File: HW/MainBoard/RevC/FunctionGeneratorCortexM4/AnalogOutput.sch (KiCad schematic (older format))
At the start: 31 parts, among them U12 TL072, U13 TL072, U5 THS7002, U9 TS12A12511DCNR

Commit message: Updated MainBoard RevC
- Block diagram and connections completed on schematic
- Need to check MCU pin availability
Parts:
- removed JP? (x2): Jumper_NO_Small, symbol Device:Jumper_NO_Small
- removed U5: THS7002, symbol PGA:THS7002
- added C13, C9: 100nF, Capacitor_SMD:C_1206_3216Metric_Pad1.42x1.75mm_HandSolder, symbol Device:C
- added C14: 10uF, Capacitor_SMD:CP_Elec_4x5.7, symbol Device:CP
- added D3, D7: D_TVS, symbol Device:D_TVS
- added R12, R13: 10K, Resistor_SMD:R_1206_3216Metric_Pad1.42x1.75mm_HandSolder, symbol Device:R
- added R16, R19, R22, R32: 1K, Resistor_SMD:R_0805_2012Metric_Pad1.15x1.40mm_HandSolder, symbol Device:R
- added R25, R33: 2K2, Resistor_SMD:R_0805_2012Metric_Pad1.15x1.40mm_HandSolder, symbol Device:R
- added R26, R34: 2K7, Resistor_SMD:R_0805_2012Metric_Pad1.15x1.40mm_HandSolder, symbol Device:R
- added R27, R35: 3K3, Resistor_SMD:R_0805_2012Metric_Pad1.15x1.40mm_HandSolder, symbol Device:R
- added R28, R36: 3K9, Resistor_SMD:R_0805_2012Metric_Pad1.15x1.40mm_HandSolder, symbol Device:R
- added R29, R37: 4K7, Resistor_SMD:R_0805_2012Metric_Pad1.15x1.40mm_HandSolder, symbol Device:R
- added R30, R38: 5K6, Resistor_SMD:R_0805_2012Metric_Pad1.15x1.40mm_HandSolder, symbol Device:R
- added R31, R39: 6K8, Resistor_SMD:R_0805_2012Metric_Pad1.15x1.40mm_HandSolder, symbol Device:R
- added R6: 560R, Resistor_SMD:R_1206_3216Metric_Pad1.42x1.75mm_HandSolder, symbol Device:R
- added TP1: TestPoint, TestPoint:TestPoint_Pad_1.0x1.0mm, symbol Connector:TestPoint
- added U10: TS5A21366, Package_SO:VSSOP-8_2.4x2.1mm_P0.5mm, symbol Analog_Switch:MAX323CPA
- added U11, U16: CD4051B, symbol Analog_Switch:CD4051B
- added U14, U15, U2, U5: DG470_1, Package_SO:MSOP-8_3x3mm_P0.65mm, symbol DG470:DG470_1
- added U7: TL072, symbol Amplifier_Operational:TL072
- gave numbers to parts that had none: 3
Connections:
- net labels added: CH1_GAIN_A, CH1_GAIN_B, CH1_GAIN_C, CH1_INVERT_MUX, CH1_OFFSET_MUX, CH1_SIGNAL, CH1_SIGNAL_OUT, CH2_GAIN_A, CH2_GAIN_B, CH2_GAIN_C, CH2_INVERT_MUX, CH2_OFFSET_MUX, CH2_SIGNAL, CH2_SIGNAL_OUT
- net labels removed: FUNC1_SIG_IN, FUNC1_SIG_OUT, FUNC1_SYNC_IN, FUNC1_SYNC_OUT, GNDS, SG0_IN, SG1_IN, SG2_IN
- wire segments 129 -> 255
- no-connect marks 7 -> 1
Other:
- note added: "0V-3V3"
- note added: "ANALOG INVERTER\n"
- note added: "DC OFFSET"
- note added: "PROGRAMMABLE\nGAIN AMPLIFIER"
- moved on the sheet: C16, C21, C26, C33, C34, R1, R10, R14, R15, R17, R18, R2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

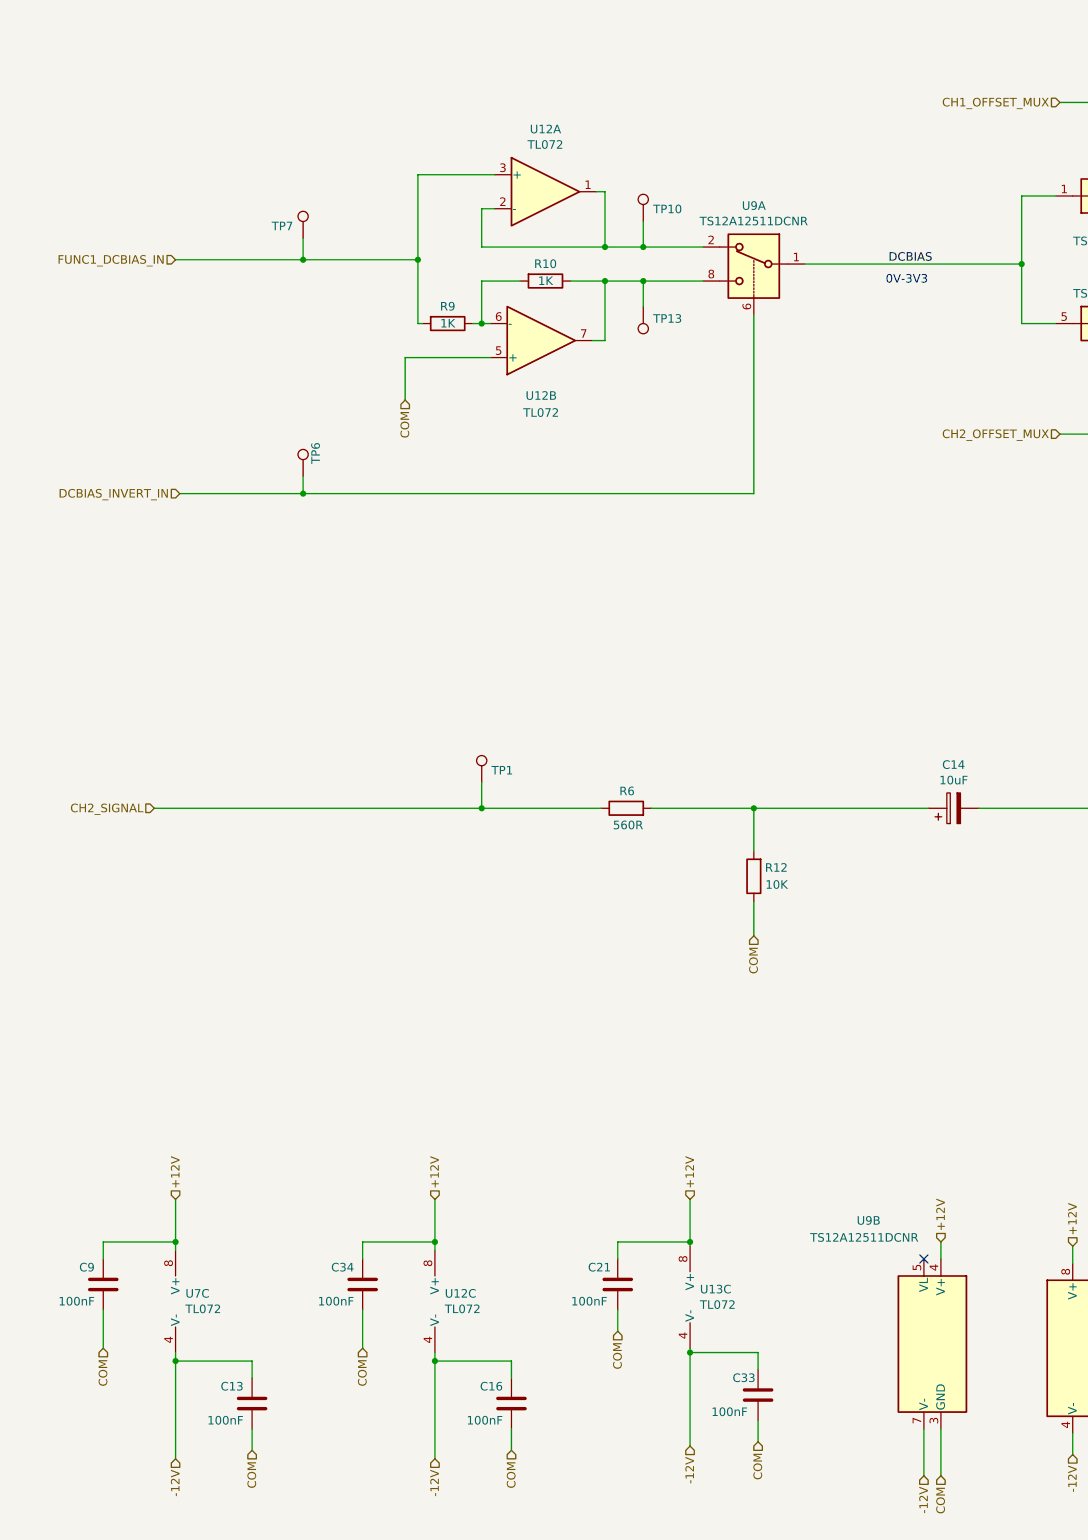
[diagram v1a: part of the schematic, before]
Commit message: Changed OFFSET SPDT to DG470
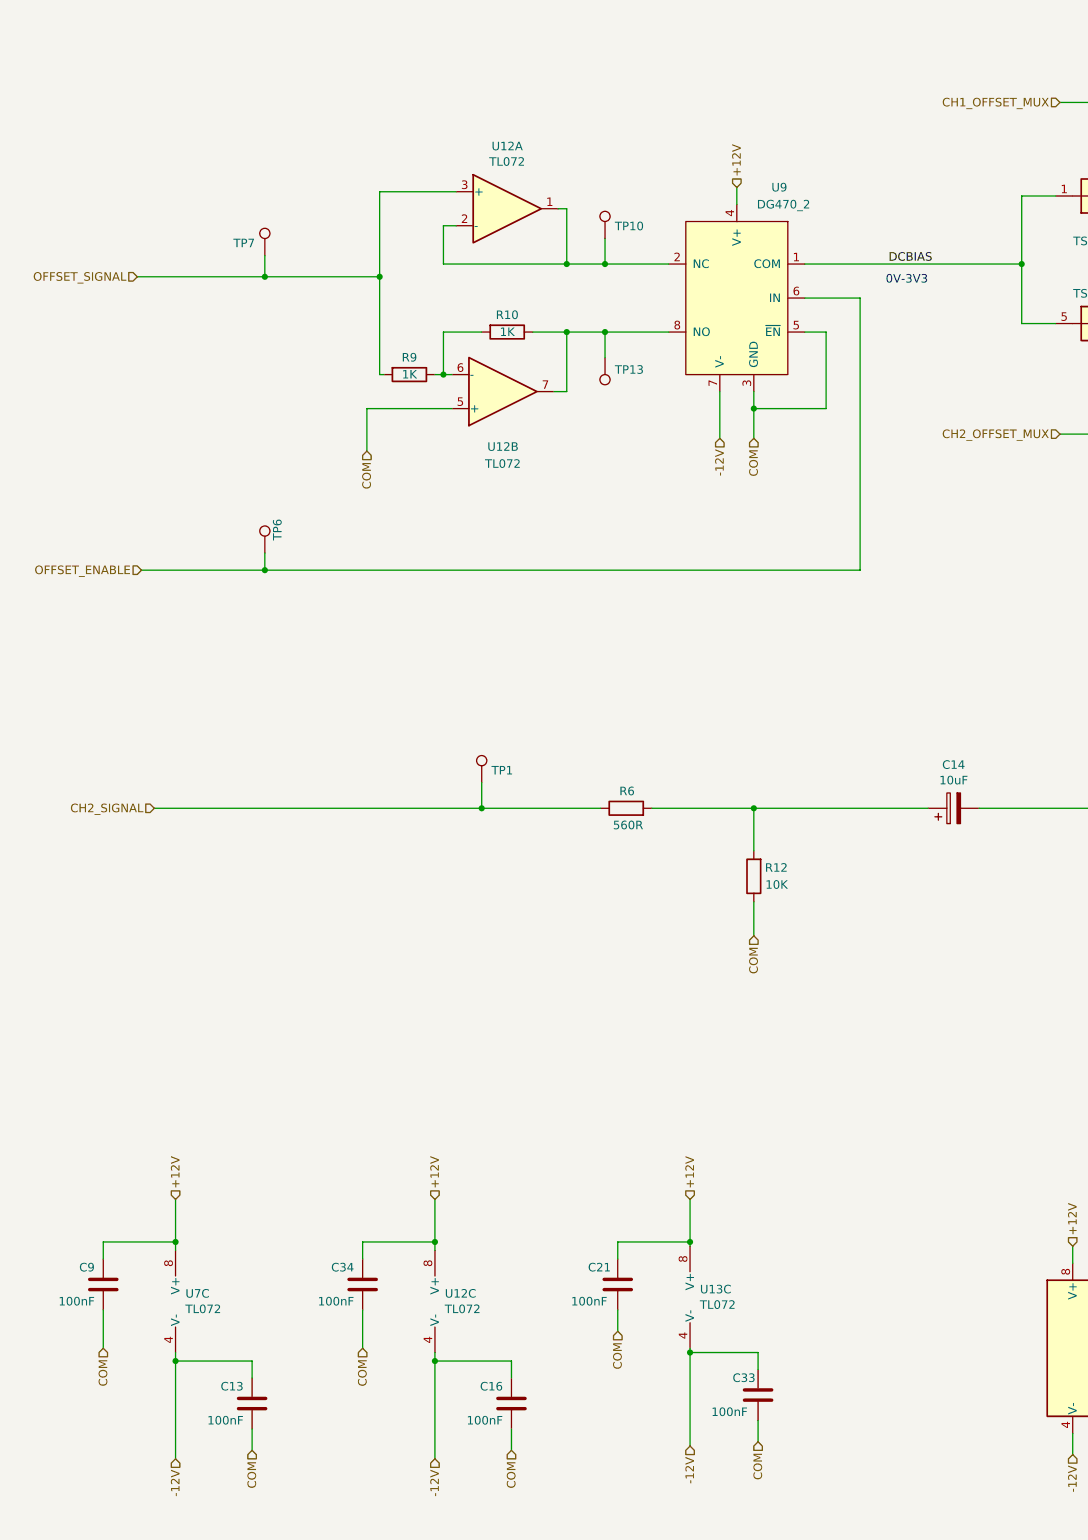
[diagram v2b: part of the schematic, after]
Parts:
- removed U9: TS12A12511DCNR, Package_TO_SOT_SMD:SOT-23-8_Handsoldering, symbol Analog_Switch:DG419LDJ
- added U9: DG470_2, Package_SO:MSOP-8_3x3mm_P0.65mm, symbol DG470:DG470_2
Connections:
- net +12V: now also U9.4 (V+)
- net -12V: now also U9.7 (V-)
- net COM: now also U9.3 (GND), U9.5 (~EN)
- net DCBIAS: now also U9.1 (COM)
- net at R10.1, TP13.1, U12.7: now also U9.8 (NO)
- net at TP10.1, U12.1, U12.2 (-): now also U9.2 (NC)
- net DCBIAS_INVERT_IN renamed OFFSET_ENABLE
- net OFFSET_ENABLE: now also U9.6 (IN)
- net FUNC1_DCBIAS_IN renamed OFFSET_SIGNAL
- no-connect marks 1 -> 0
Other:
- moved on the sheet: R10, R9, TP10, TP13, TP6, TP7, U12A, U12B

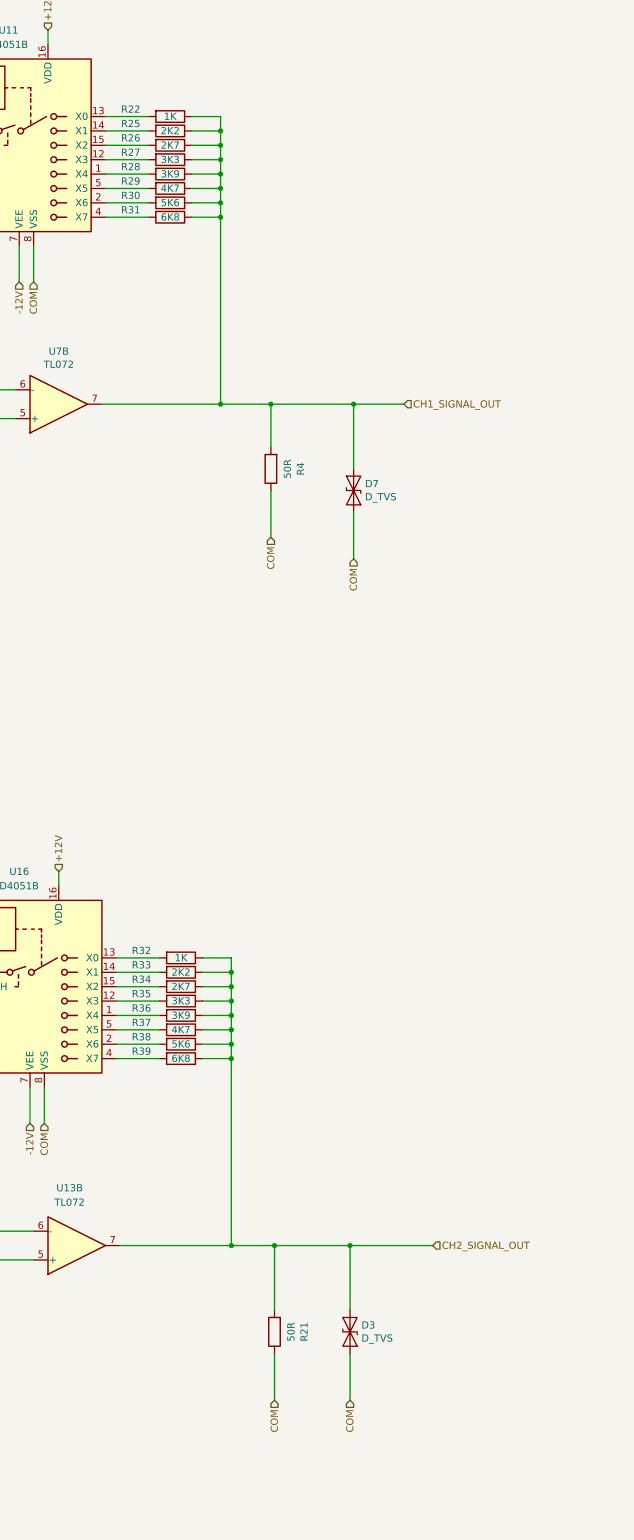
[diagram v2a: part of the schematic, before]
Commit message: Added two-series resistors in PGA feedback
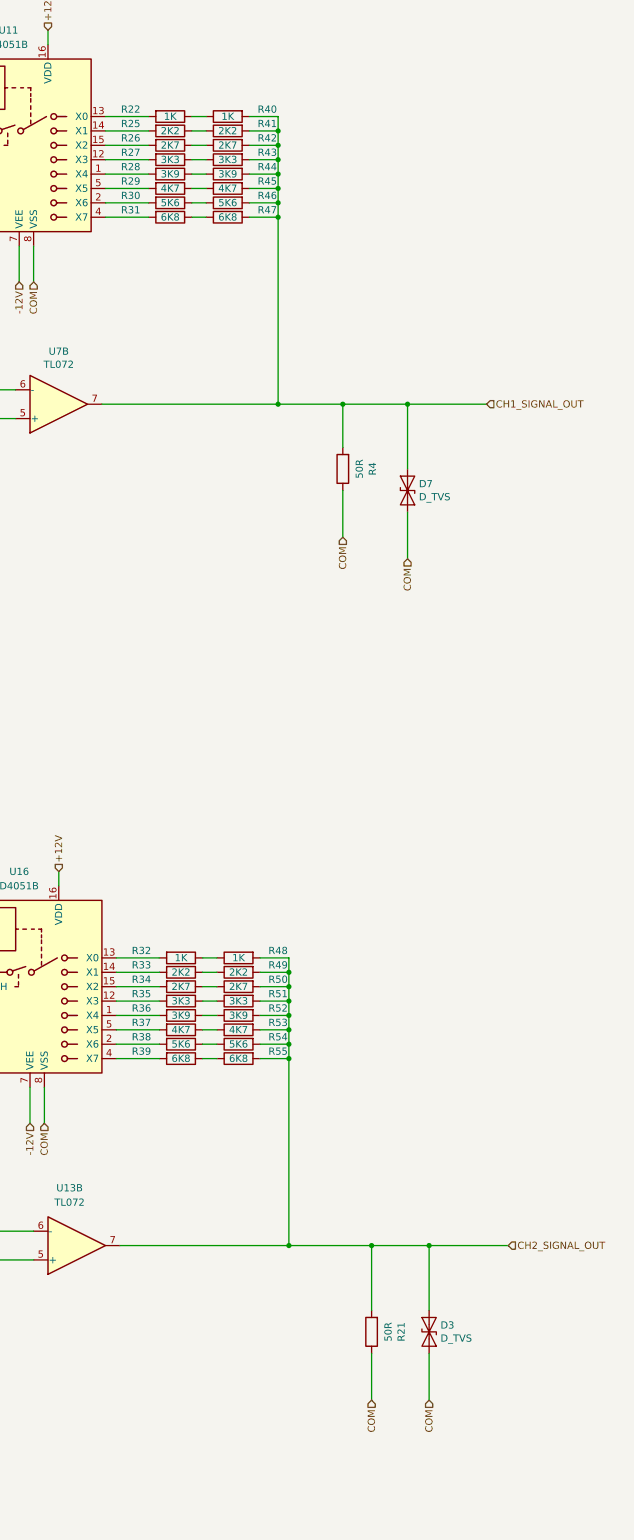
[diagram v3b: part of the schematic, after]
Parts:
- added R40, R48: 1K, Resistor_SMD:R_0805_2012Metric_Pad1.15x1.40mm_HandSolder, symbol Device:R
- added R41, R49: 2K2, Resistor_SMD:R_0805_2012Metric_Pad1.15x1.40mm_HandSolder, symbol Device:R
- added R42, R50: 2K7, Resistor_SMD:R_0805_2012Metric_Pad1.15x1.40mm_HandSolder, symbol Device:R
- added R43, R51: 3K3, Resistor_SMD:R_0805_2012Metric_Pad1.15x1.40mm_HandSolder, symbol Device:R
- added R44, R52: 3K9, Resistor_SMD:R_0805_2012Metric_Pad1.15x1.40mm_HandSolder, symbol Device:R
- added R45, R53: 4K7, Resistor_SMD:R_0805_2012Metric_Pad1.15x1.40mm_HandSolder, symbol Device:R
- added R46, R54: 5K6, Resistor_SMD:R_0805_2012Metric_Pad1.15x1.40mm_HandSolder, symbol Device:R
- added R47, R55: 6K8, Resistor_SMD:R_0805_2012Metric_Pad1.15x1.40mm_HandSolder, symbol Device:R
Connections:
- net CH1_SIGNAL_OUT: now also R40.2, R41.2, R42.2, R43.2, R44.2, R45.2, R46.2, R47.2; no longer R22.1, R25.1, R26.1, R27.1, R28.1, R29.1, R30.1, R31.1
- net CH2_SIGNAL_OUT: now also R48.2, R49.2, R50.2, R51.2, R52.2, R53.2, R54.2, R55.2; no longer R32.1, R33.1, R34.1, R35.1, R36.1, R37.1, R38.1, R39.1
- new net: R22.1, R40.1
- new net: R25.1, R41.1
- new net: R26.1, R42.1
- new net: R27.1, R43.1
- new net: R28.1, R44.1
- new net: R29.1, R45.1
- new net: R30.1, R46.1
- new net: R31.1, R47.1
- new net: R32.1, R48.1
- new net: R33.1, R49.1
- new net: R34.1, R50.1
- new net: R35.1, R51.1
- new net: R36.1, R52.1
- new net: R37.1, R53.1
- new net: R38.1, R54.1
- new net: R39.1, R55.1
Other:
- moved on the sheet: D3, D7, R21, R4

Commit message: Created RevE ControlBoard to use 2.54 SMD header
Header is at the top of the board to let buttons and encoder be closer together
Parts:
- removed unit 1 of U10
- removed unit 2 of U10
- added U? (x2): DG468DV_T1_E3, Package_SO:TSOP-6_1.65x3.05mm_P0.95mm, symbol DG46x:DG468DV_T1_E3
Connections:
- net +12V: now also U?.5 (V+), U?.5 (V+)
- net -12V: now also U?.2 (V-), U?.2 (V-)
- net CH1_OFFSET_MUX: now also U?.3 (IN)
- net CH2_OFFSET_MUX: now also U?.3 (IN)
- net COM: now also U?.4 (GND), U?.4 (GND)
- net DCBIAS: now also U?.1 (NO), U?.1 (NO)
- net at R3.2: now also U?.6 (COM)
- net at R13.1: now also U?.6 (COM)
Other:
- note added: "-3V3 -> +3V3"
- note added: "± 15 V analog signal range"
- note removed: "0V-3V3"
- moved on the sheet: C14, C26, R1, R10, R12, R2, R6, R9, TP1, TP10, TP13, TP6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

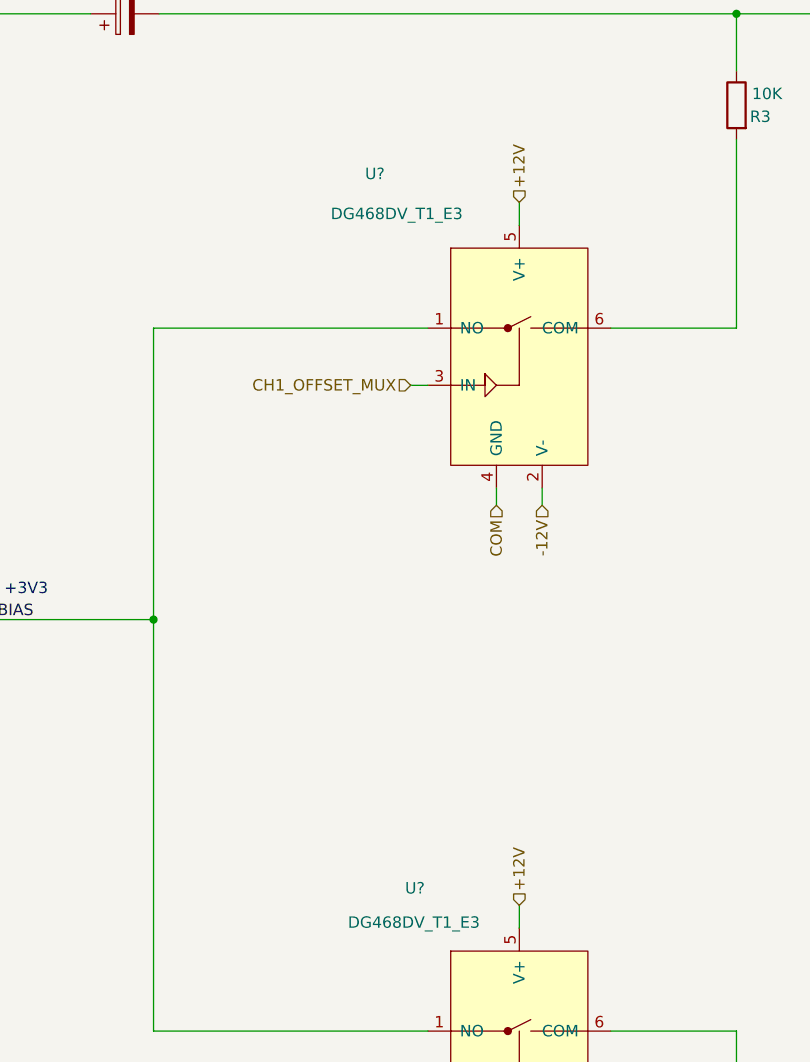
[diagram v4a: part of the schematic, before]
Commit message: Created Front Panel board layout
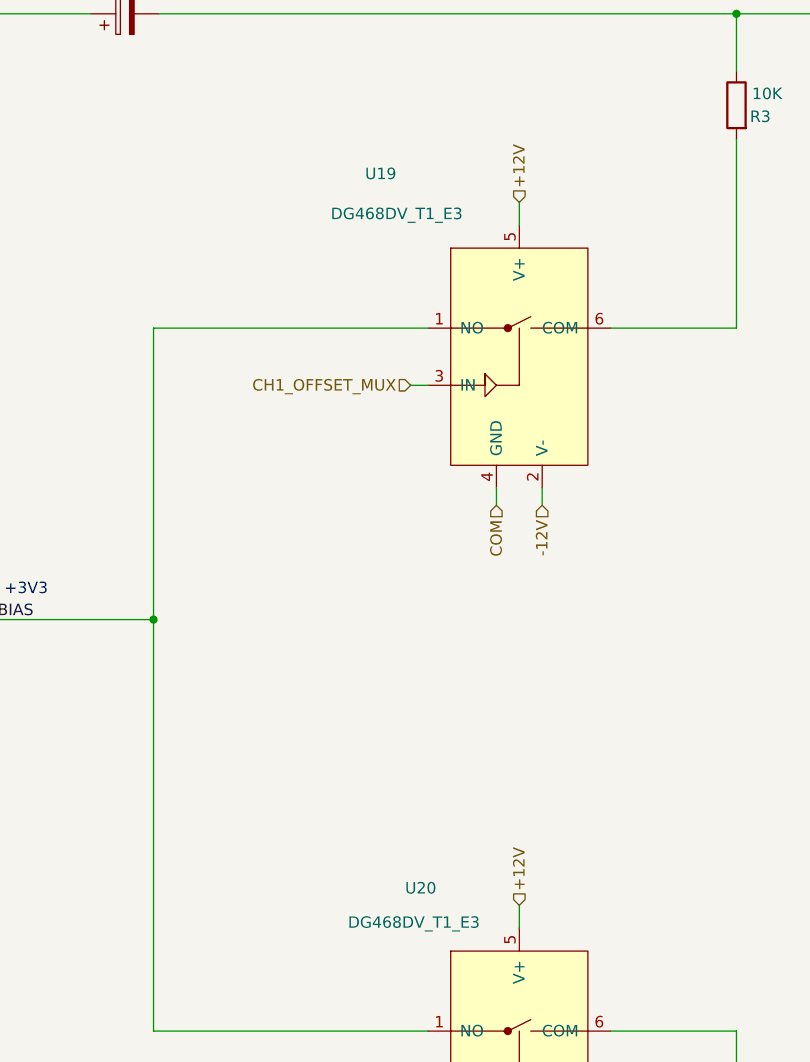
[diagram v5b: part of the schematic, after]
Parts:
- gave numbers to parts that had none: 2
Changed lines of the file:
@@
 ± 15 V analog signal range
 $Comp
-L DG46x:DG468DV_T1_E3 U?
+L DG46x:DG468DV_T1_E3 U19
 U 1 1 5F061CB7
 P 7625 7175
-F 0 "U?" H 6950 7950 50  0000 L CNN
+F 0 "U19" H 6950 7950 50  0000 L CNN
 F 1 "DG468DV_T1_E3" H 6800 7775 50  0000 L CNN
 F 2 "Package_SO:TSOP-6_1.65x3.05mm_P0.95mm" H 7625 7225 50  0001 C CNN
@@
 	8025 10150 8575 10150
 $Comp
-L DG46x:DG468DV_T1_E3 U?
+L DG46x:DG468DV_T1_E3 U20
 U 1 1 5F203717
 P 7625 10250
-F 0 "U?" H 7125 10975 50  0000 L CNN
+F 0 "U20" H 7125 10975 50  0000 L CNN
 F 1 "DG468DV_T1_E3" H 6875 10825 50  0000 L CNN
 F 2 "Package_SO:TSOP-6_1.65x3.05mm_P0.95mm" H 7625 10300 50  0001 C CNN
